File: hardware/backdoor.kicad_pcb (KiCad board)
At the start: 2 copper layers, 81.3 x 61 mm, 30 parts, among them J1 E1, Q1 J201, U1 OP07

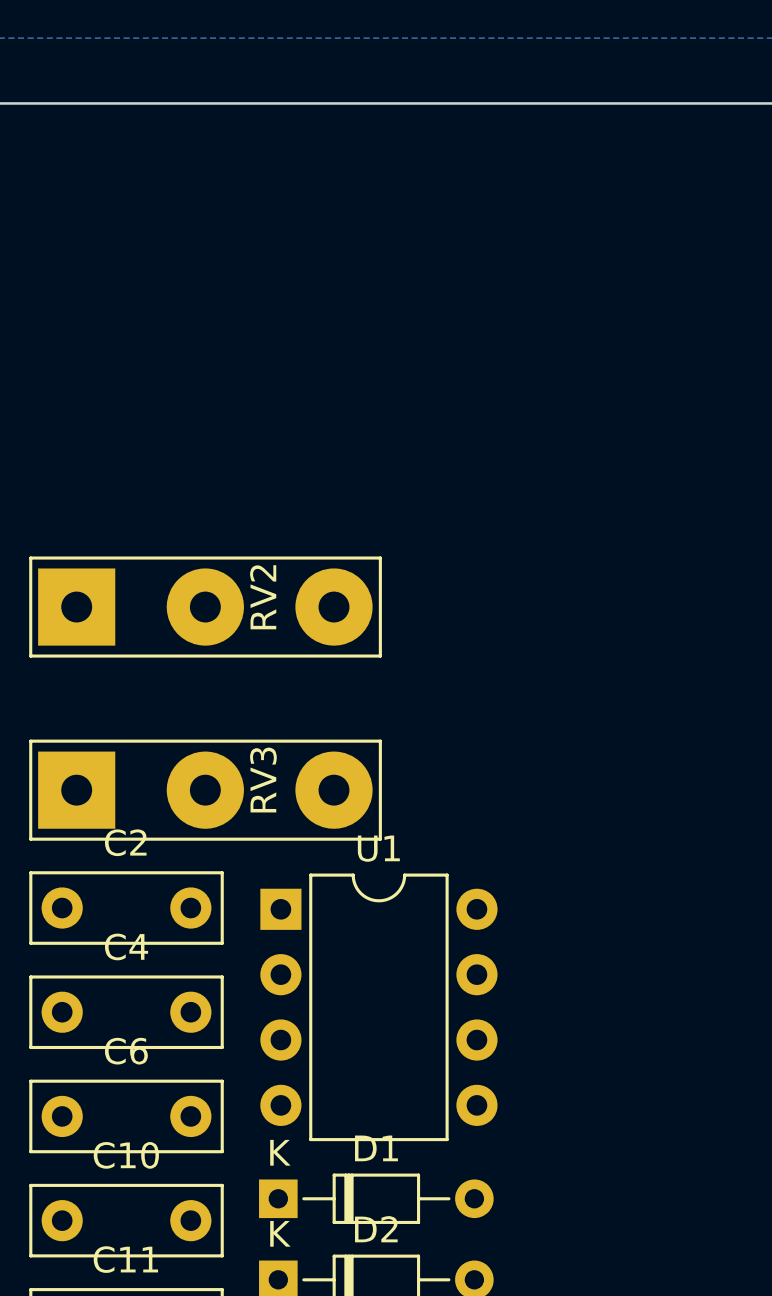
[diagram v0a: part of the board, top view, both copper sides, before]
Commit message: Add values after experimenting on the breadboard
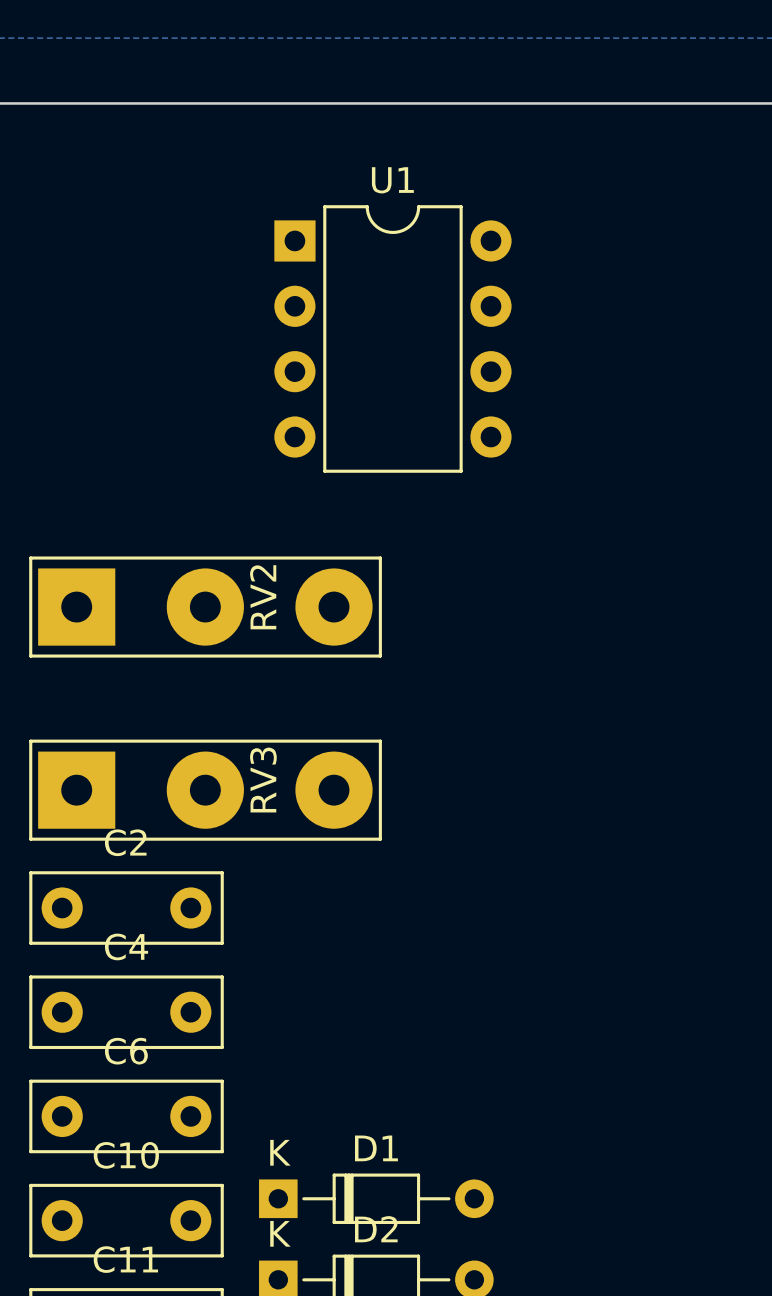
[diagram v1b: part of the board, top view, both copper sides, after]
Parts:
- C10: value C -> 22p
- C11: value C -> 3n3
- C12: value C -> 22n
- C13: value C_Polarized -> 1u
- C2: value C -> 1n
- C4: value C -> 2n2
- C6: value C -> 100p
- C7: value C_Polarized -> 2u2
- C8, C9: value C_Polarized -> 4u7
- D1, D2: value D -> 1N914
- R10: value R_US -> 1k5
- R11: value R_US -> 10K
- R3, R4, R5: value R_US -> 1M
- R6, R9: value R_US -> 1K
- R7: value R_US -> 47
- R8: value R_US -> 270
- moved U1 26.0 mm to (109.9, 28.2)
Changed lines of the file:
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@@
         (effects (font (size 1 1) (thickness 0.15)))
     )
-    (fp_text value "R_US" (at 3.81 2.37) (layer "F.Fab")
+    (fp_text value "1M" (at 3.81 2.37) (layer "F.Fab")
         (effects (font (size 1 1) (thickness 0.15)))
     )
@@
         (effects (font (size 1 1) (thickness 0.15)))
     )
-    (fp_text value "C_Polarized" (at 1.25 3.75) (layer "F.Fab")
+    (fp_text value "4u7" (at 1.25 3.75) (layer "F.Fab")
         (effects (font (size 1 1) (thickness 0.15)))
     )
@@
         (effects (font (size 1 1) (thickness 0.15)))
     )
-    (fp_text value "R_US" (at 3.81 2.37) (layer "F.Fab")
+    (fp_text value "1K" (at 3.81 2.37) (layer "F.Fab")
         (effects (font (size 1 1) (thickness 0.15)))
     )
@@
         (effects (font (size 1 1) (thickness 0.15)))
     )
-    (fp_text value "C_Polarized" (at 1.25 3.75) (layer "F.Fab")
+    (fp_text value "2u2" (at 1.25 3.75) (layer "F.Fab")
         (effects (font (size 1 1) (thickness 0.15)))
     )
@@
         (effects (font (size 1 1) (thickness 0.15)))
     )
-    (fp_text value "C" (at 2.5 2.5) (layer "F.Fab")
+    (fp_text value "1n" (at 2.5 2.5) (layer "F.Fab")
         (effects (font (size 1 1) (thickness 0.15)))
     )
@@
         (effects (font (size 1 1) (thickness 0.15)))
     )
-    (fp_text value "D" (at 3.81 1.92) (layer "F.Fab")
+    (fp_text value "1N914" (at 3.81 1.92) (layer "F.Fab")
         (effects (font (size 1 1) (thickness 0.15)))
     )
@@
         (effects (font (size 1 1) (thickness 0.15)))
     )
-    (fp_text value "C" (at 2.5 2.5) (layer "F.Fab")
+    (fp_text value "3n3" (at 2.5 2.5) (layer "F.Fab")
         (effects (font (size 1 1) (thickness 0.15)))
     )
@@
         (effects (font (size 1 1) (thickness 0.15)))
     )
-    (fp_text value "C_Polarized" (at 1.25 3.75) (layer "F.Fab")
+    (fp_text value "4u7" (at 1.25 3.75) (layer "F.Fab")
         (effects (font (size 1 1) (thickness 0.15)))
     )
@@
         (effects (font (size 1 1) (thickness 0.15)))
     )
-    (fp_text value "R_US" (at 3.81 2.37) (layer "F.Fab")
+    (fp_text value "1k5" (at 3.81 2.37) (layer "F.Fab")
         (effects (font (size 1 1) (thickness 0.15)))
     )
@@
         (effects (font (size 1 1) (thickness 0.15)))
     )
-    (fp_text value "C" (at 2.5 2.5) (layer "F.Fab")
+    (fp_text value "2n2" (at 2.5 2.5) (layer "F.Fab")
         (effects (font (size 1 1) (thickness 0.15)))
     )
@@
         (effects (font (size 1 1) (thickness 0.15)))
     )
-    (fp_text value "C" (at 2.5 2.5) (layer "F.Fab")
+    (fp_text value "22n" (at 2.5 2.5) (layer "F.Fab")
         (effects (font (size 1 1) (thickness 0.15)))
     )
@@
         (effects (font (size 1 1) (thickness 0.15)))
     )
-    (fp_text value "C" (at 2.5 2.5) (layer "F.Fab")
+    (fp_text value "100p" (at 2.5 2.5) (layer "F.Fab")
         (effects (font (size 1 1) (thickness 0.15)))
     )
@@
         (effects (font (size 1 1) (thickness 0.15)))
     )
-    (fp_text value "R_US" (at 3.81 2.37) (layer "F.Fab")
+    (fp_text value "47" (at 3.81 2.37) (layer "F.Fab")
         (effects (font (size 1 1) (thickness 0.15)))
     )
@@
         (effects (font (size 1 1) (thickness 0.15)))
     )
-    (fp_text value "R_US" (at 3.81 2.37) (layer "F.Fab")
+    (fp_text value "270" (at 3.81 2.37) (layer "F.Fab")
         (effects (font (size 1 1) (thickness 0.15)))
     )
@@
         (effects (font (size 1 1) (thickness 0.15)))
     )
-    (fp_text value "R_US" (at 3.81 2.37) (layer "F.Fab")
+    (fp_text value "10K" (at 3.81 2.37) (layer "F.Fab")
         (effects (font (size 1 1) (thickness 0.15)))
     )
@@
         (effects (font (size 1 1) (thickness 0.15)))
     )
-    (fp_text value "R_US" (at 3.81 2.37) (layer "F.Fab")
+    (fp_text value "1K" (at 3.81 2.37) (layer "F.Fab")
         (effects (font (size 1 1) (thickness 0.15)))
     )
@@
         (effects (font (size 1 1) (thickness 0.15)))
     )
-    (fp_text value "D" (at 3.81 1.92) (layer "F.Fab")
+    (fp_text value "1N914" (at 3.81 1.92) (layer "F.Fab")
         (effects (font (size 1 1) (thickness 0.15)))
     )
@@
   )
   (footprint "Package_DIP:DIP-8_W7.62mm" (layer "F.Cu")
-    (at 109.32 54.18)
+    (at 109.865 28.204)
     (descr "8-lead though-hole mounted DIP package, row spacing 7.62 mm (300 mils)")
     (tags "THT DIP DIL PDIP 2.54mm 7.62mm 300mil")
@@
         (effects (font (size 1 1) (thickness 0.15)))
     )
-    (fp_text value "C" (at 2.5 2.5) (layer "F.Fab")
+    (fp_text value "22p" (at 2.5 2.5) (layer "F.Fab")
         (effects (font (size 1 1) (thickness 0.15)))
     )
@@
         (effects (font (size 1 1) (thickness 0.15)))
     )
-    (fp_text value "R_US" (at 3.81 2.37) (layer "F.Fab")
+    (fp_text value "1M" (at 3.81 2.37) (layer "F.Fab")
         (effects (font (size 1 1) (thickness 0.15)))
     )
@@
         (effects (font (size 1 1) (thickness 0.15)))
     )
-    (fp_text value "R_US" (at 3.81 2.37) (layer "F.Fab")
+    (fp_text value "1M" (at 3.81 2.37) (layer "F.Fab")
         (effects (font (size 1 1) (thickness 0.15)))
     )
@@
         (effects (font (size 1 1) (thickness 0.15)))
     )
-    (fp_text value "C_Polarized" (at 1.25 3.75) (layer "F.Fab")
-        (effects (font (size 1 1) (thickness 0.15)))
-    )
+    (fp_text value "1u" (at 1.25 3.75) (layer "F.Fab")
+        (effects (font (size 1 1) (thickness 0.15)))
+    )

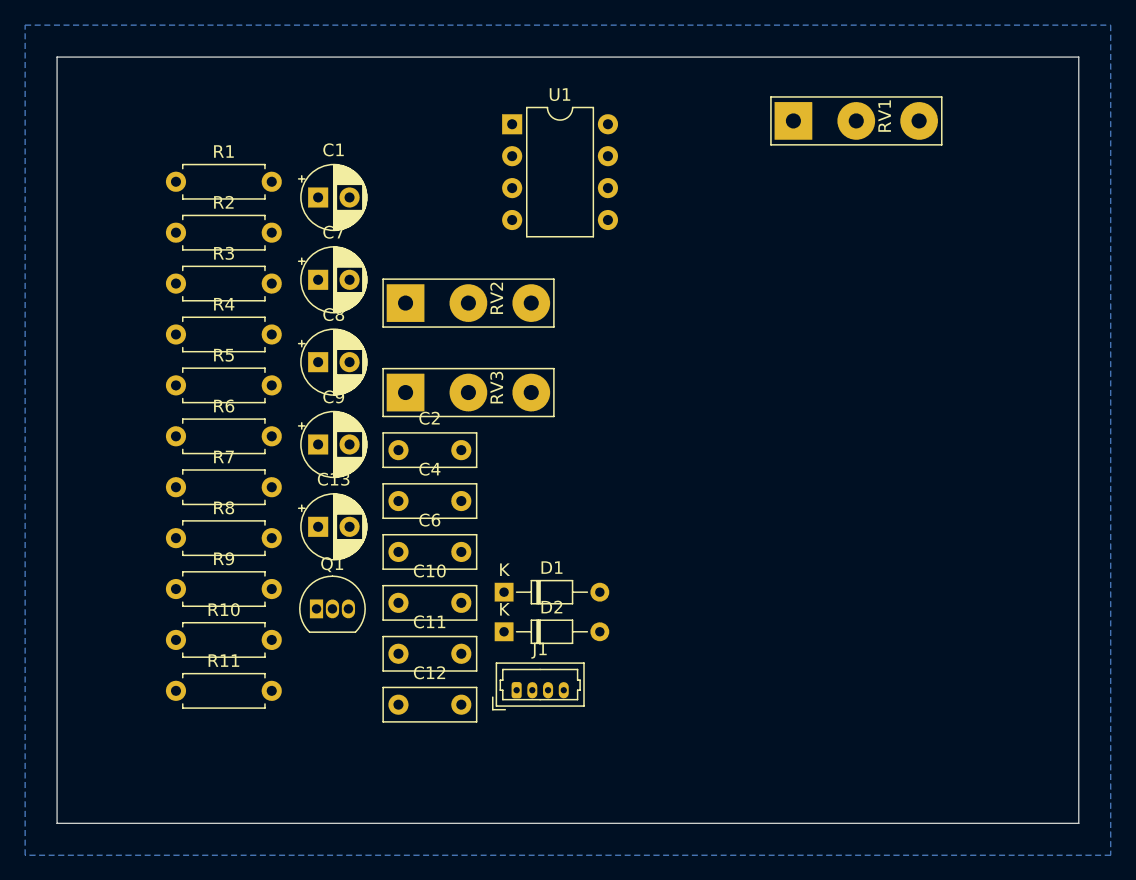
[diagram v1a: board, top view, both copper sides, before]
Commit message: initial layout and renders, bump rev to v0.02
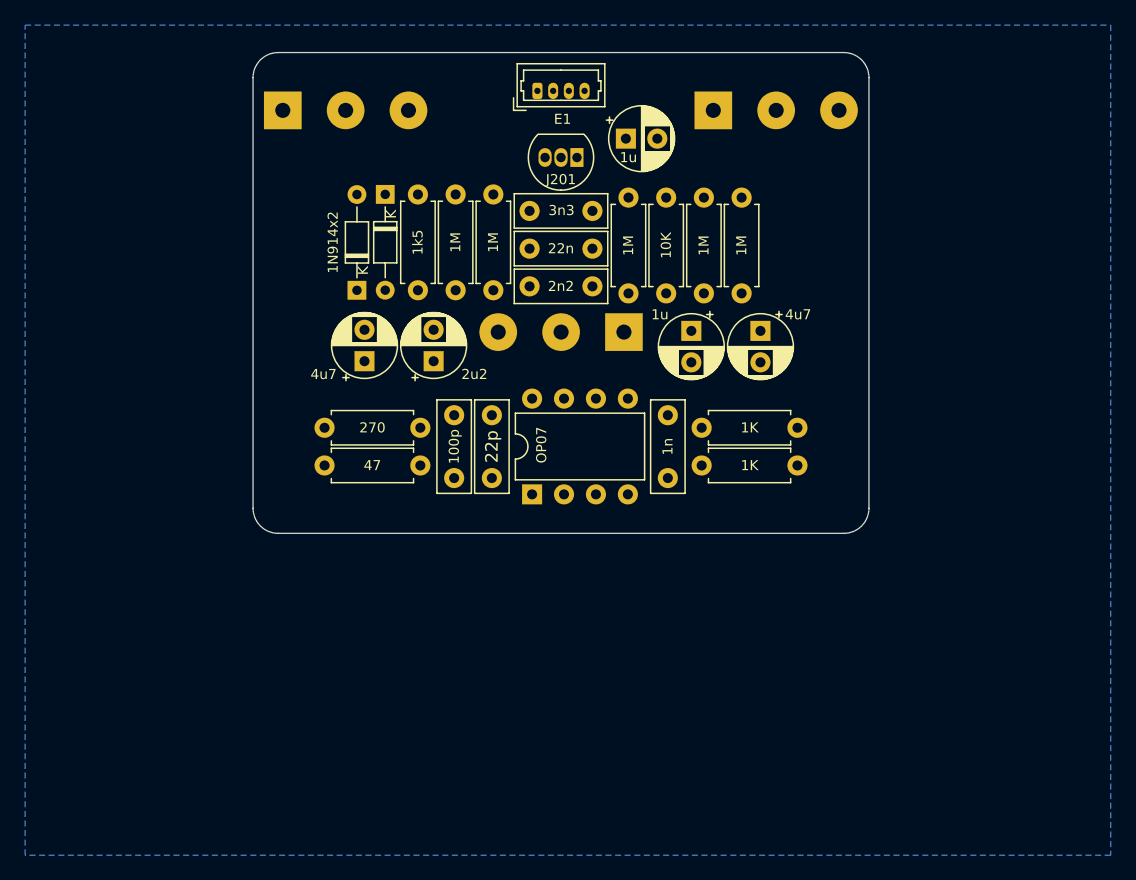
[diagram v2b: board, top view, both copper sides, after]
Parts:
- RV1, RV2, RV3: value 100K -> A100K; moved to B.Cu
- moved R11 55.3 mm to (122.1, 34.0), turned to -90 degrees
- moved R9 50.4 mm to (132.6, 55.4), turned to 180 degrees
- moved J1 47.7 mm to (111.9, 25.6)
- moved R2 45.1 mm to (128.1, 34.0), turned to -90 degrees
- moved R1 42.9 mm to (125.1, 41.7), turned to 90 degrees
- moved R6 41.8 mm to (124.9, 52.4)
- moved Q1 41.5 mm to (115.0, 30.9), turned to 180 degrees
- moved R10 40.3 mm to (102.4, 33.8), turned to -90 degrees
- moved C13 39.4 mm to (118.9, 29.4)
- moved R5 39.0 mm to (119.1, 34.0), turned to -90 degrees
- moved C12 37.7 mm to (111.2, 38.1)
- moved C11 36.7 mm to (111.2, 35.1)
- moved C9 36.3 mm to (129.6, 44.6), turned to -90 degrees
- moved D1 33.0 mm to (99.8, 33.8), turned to -90 degrees
- moved C1 31.5 mm to (124.1, 44.6), turned to -90 degrees
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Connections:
- net Net-(C10-Pad1) renamed /OA_Comp2
- net Net-(C10-Pad2) renamed /OA_Comp1
- net Net-(C13-Pad2) renamed /Pre-Volume
- net Net-(C4-Pad2) renamed /DC_Biased
- net Net-(C6-Pad2) renamed /OA_Out
- net Net-(D1-A) renamed /Clip
- net Net-(Q1-D) renamed /Buffer_Out
- net Net-(Q1-G) renamed /Pre-Buffer
- net Net-(U1-+) renamed /OA_NonInv
- net Net-(U1--) renamed /OA_Inv
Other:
- board size 81.3 x 61 mm -> 49 x 38.2 mm
- board text added: "${COMMENT1} ${REVISION}"

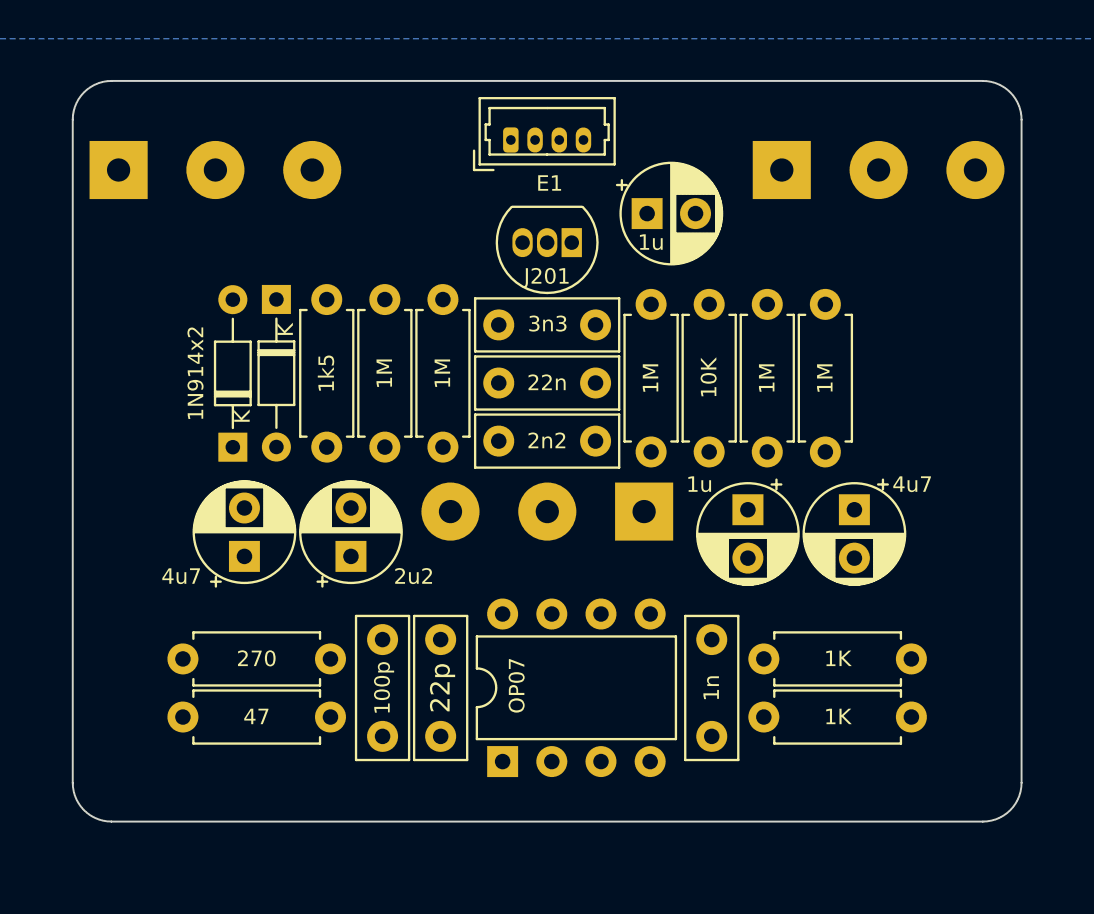
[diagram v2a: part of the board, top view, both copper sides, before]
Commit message: Routed v0.02, ready for fabrication
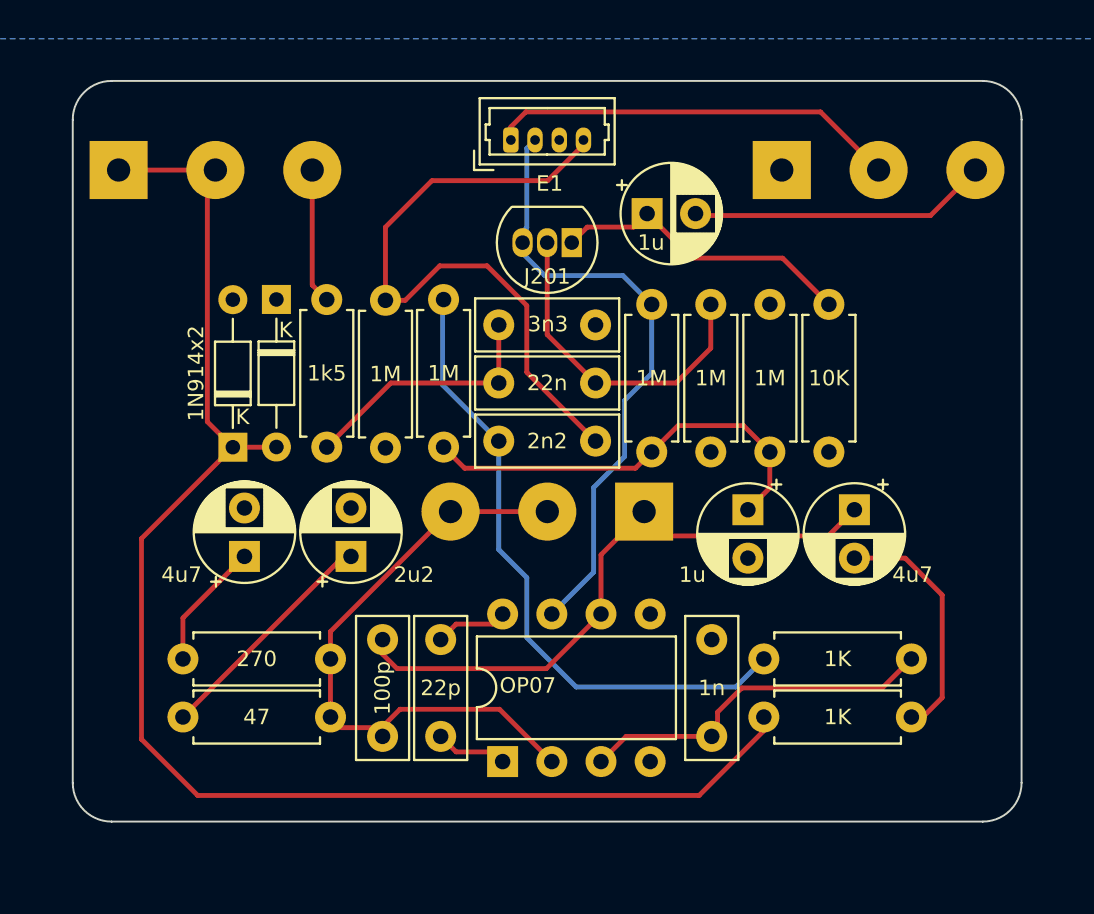
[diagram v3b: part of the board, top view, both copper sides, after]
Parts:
- moved R3 7.58 mm to (105.4, 33.8), turned to -90 degrees
- moved R11 6.18 mm to (128.3, 34.0)
- moved R1 5.97 mm to (119.2, 41.7)
- moved R5 3.08 mm to (122.2, 34.0)
- moved R2 2.87 mm to (125.2, 34.0)
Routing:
- net /Clip: track 0.00 -> 74.8 mm
- net /EFFECT_IN: track 0.00 -> 33.4 mm
- net /DC_Biased: track 0.00 -> 33.2 mm
- net /OA_Inv: track 0.00 -> 32.1 mm
- net /9V0: track 0.00 -> 32.0 mm
- net /OA_Out: track 0.00 -> 31.7 mm
- net /VREF: track 0.00 -> 22.2 mm
- net /EFFECT_OUT: track 0.00 -> 21.2 mm
- net /OA_NonInv: track 0.00 -> 18.8 mm
- net /Pre-Buffer: track 0.00 -> 17.2 mm
- net /Buffer_Out: track 0.00 -> 15.8 mm
- net /Pre-Volume: track 0.00 -> 15.5 mm
- net Net-(C11-Pad1): track 0.00 -> 13.3 mm
- net Net-(C9-Pad2): track 0.00 -> 12.6 mm
- net Net-(C7-Pad1): track 0.00 -> 12.1 mm
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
